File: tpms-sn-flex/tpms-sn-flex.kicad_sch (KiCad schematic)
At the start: 28 parts, among them IC1 NPP-301A-700AT, J1 Conn_02x04_Odd_Even, J2 Conn_01x04, J3 SMA Female, SW1 SW_Push, U1 STM32U031R8T6

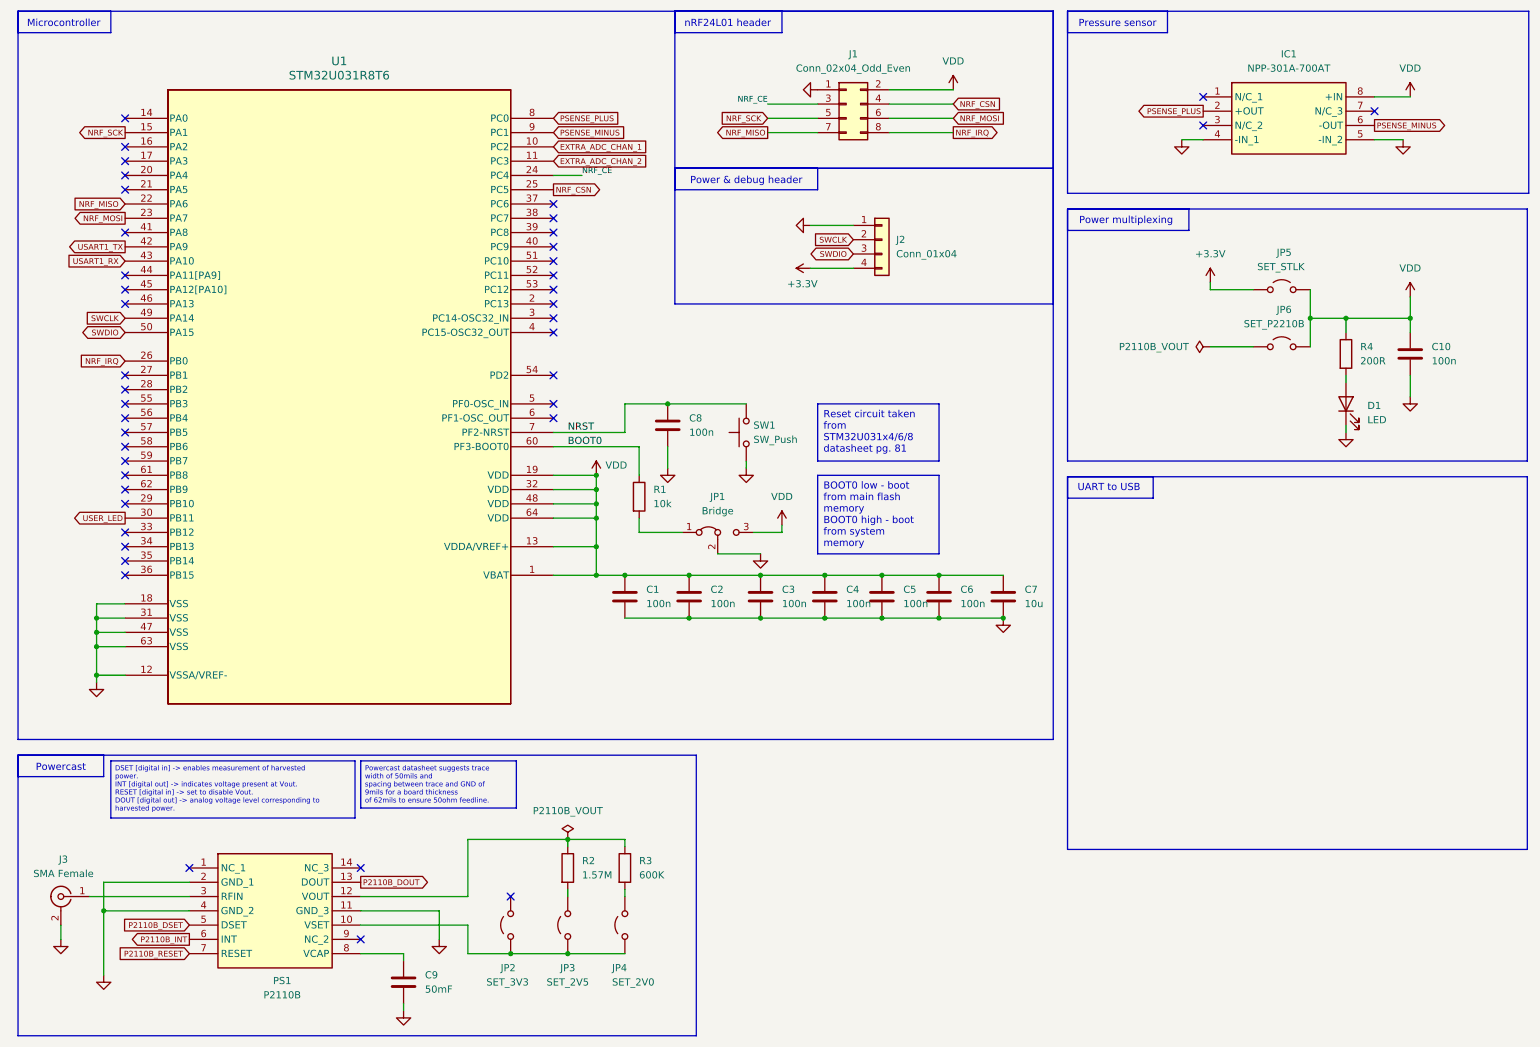
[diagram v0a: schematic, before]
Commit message: Add layout and routing for sensor node PCB rev 1
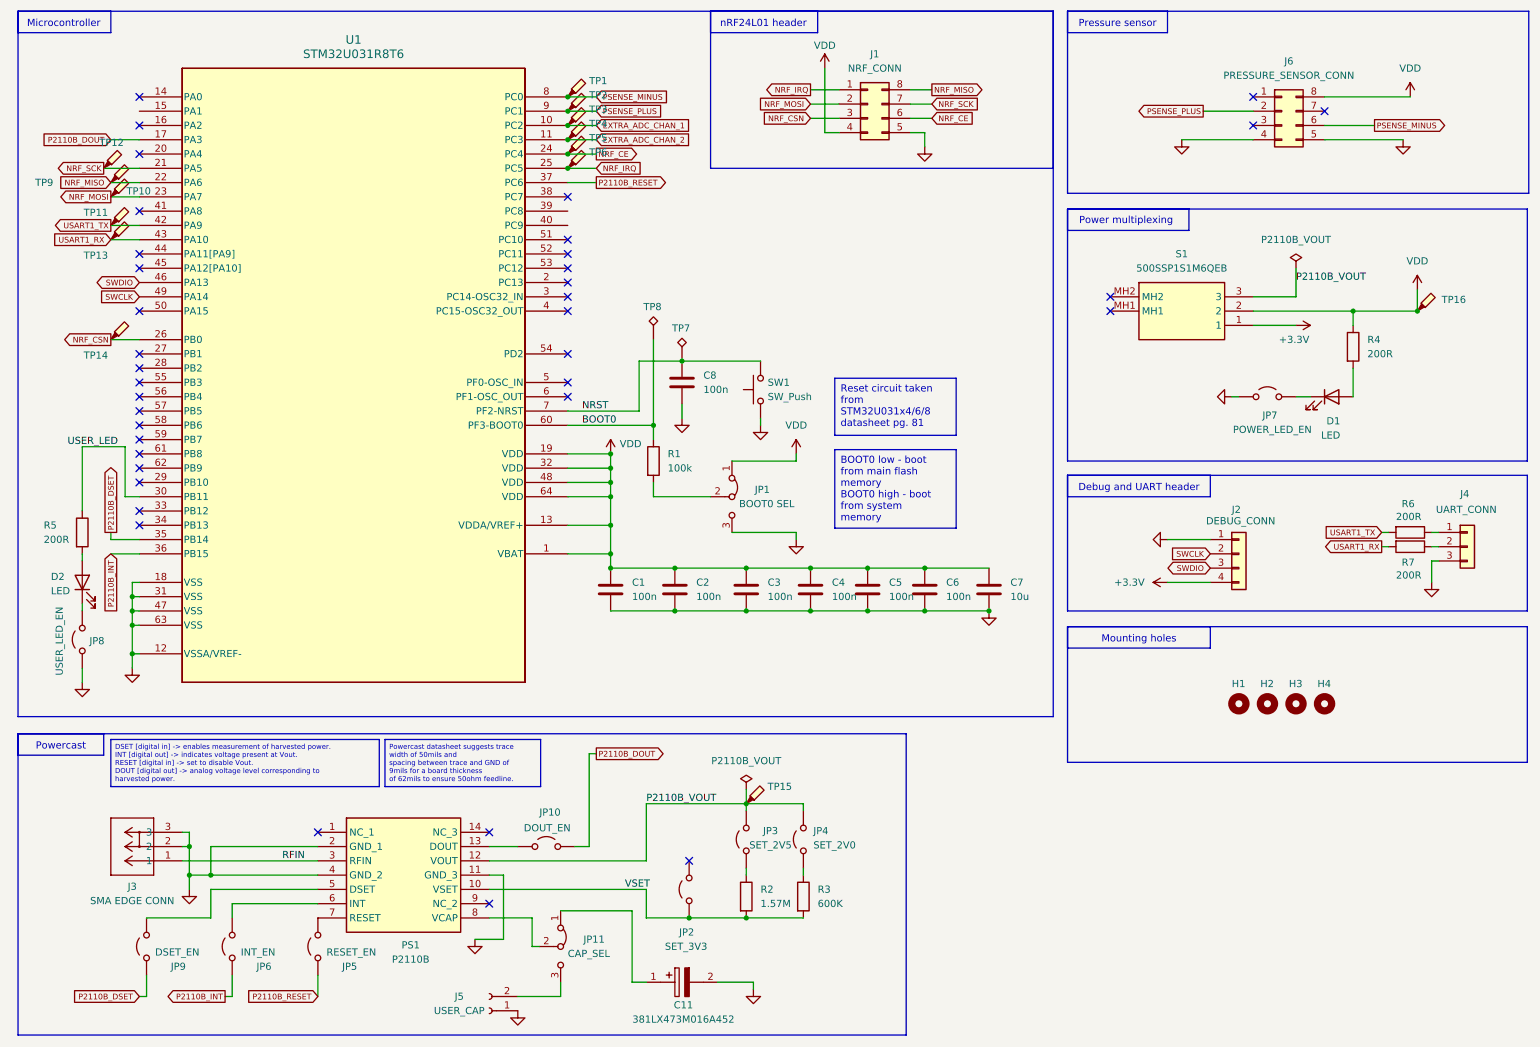
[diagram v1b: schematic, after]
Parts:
- removed C10: 100n, Capacitor_SMD:C_01005_0402Metric, symbol Device:C
- removed C9: 50mF, Capacitor_SMD:C_01005_0402Metric, symbol Device:C
- removed IC1: NPP-301A-700AT, libtpms:SOIC127P610X280-8N, symbol libtpms:NPP-301A-700AT
- removed J1: Conn_02x04_Odd_Even, Connector_PinHeader_2.54mm:PinHeader_2x04_P2.54mm_Vertical, symbol Connector_Generic:Conn_02x04_Odd_Even
- removed J3: SMA Female, symbol Connector:Conn_Coaxial
- added C11: 381LX473M016A452, libtpms:CAPPRD1000W200D3550H4700, symbol libtpms:381LX473M016A452
- added D2: LED, LED_SMD:LED_0402_1005Metric, symbol Device:LED
- added H1, H2, H3, H4: MountingHole, MountingHole:MountingHole_2.2mm_M2, symbol Mechanical:MountingHole
- added J1: NRF_CONN, Connector_PinSocket_2.54mm:PinSocket_2x04_P2.54mm_Vertical, symbol Connector_Generic:Conn_02x04_Counter_Clockwise
- added J3: SMA EDGE CONN, libtpms:CONN_73251-1150_MOL, symbol libtpms:732511150
- added J4: UART_CONN, Connector_PinHeader_2.54mm:PinHeader_1x03_P2.54mm_Vertical, symbol Connector_Generic:Conn_01x03
- added J5: USER_CAP, Connector_PinSocket_2.54mm:PinSocket_1x02_P2.54mm_Vertical, symbol Connector:Conn_01x02_Socket
- added J6: PRESSURE_SENSOR_CONN, libtpms:8-SOIC-DIP-8-ADAPTER, symbol Connector_Generic:Conn_02x04_Counter_Clockwise
- added JP10: DOUT_EN, Connector_PinHeader_2.54mm:PinHeader_1x02_P2.54mm_Vertical, symbol Jumper:Jumper_2_Open
- added JP11: CAP_SEL, Connector_PinHeader_2.54mm:PinHeader_1x03_P2.54mm_Vertical, symbol Jumper:Jumper_3_Bridged12
- added JP7: POWER_LED_EN, Connector_PinHeader_2.54mm:PinHeader_1x02_P2.54mm_Vertical, symbol Jumper:Jumper_2_Open
- added JP8: USER_LED_EN, Connector_PinHeader_2.54mm:PinHeader_1x02_P2.54mm_Vertical, symbol Jumper:Jumper_2_Open
- added JP9: DSET_EN, Connector_PinHeader_2.54mm:PinHeader_1x02_P2.54mm_Vertical, symbol Jumper:Jumper_2_Open
- added R5, R6, R7: 200R, Resistor_SMD:R_0603_1608Metric, symbol Device:R
- added S1: 500SSP1S1M6QEB, libtpms:500SSP1S1M6QEB, symbol libtpms:500SSP1S1M6QEB
- added TP1, TP2, TP3, TP4, TP5, TP6: TestPoint_Probe, TestPoint:TestPoint_Pad_2.0x2.0mm, symbol Connector:TestPoint_Probe
- added TP10, TP11, TP12, TP13, TP14, TP15, TP16, TP9: ~, TestPoint:TestPoint_Pad_2.0x2.0mm, symbol Connector:TestPoint_Probe
- added TP7, TP8: TestPoint_Alt, TestPoint:TestPoint_Pad_2.0x2.0mm, symbol Connector:TestPoint_Alt
- C7: footprint Capacitor_SMD:C_01005_0402Metric -> Capacitor_SMD:C_0201_0603Metric
- J2: value Conn_01x04 -> DEBUG_CONN
- JP1: value Bridge -> BOOT0 SEL; footprint TestPoint:TestPoint_Bridge_Pitch2.54mm_Drill1.0mm -> Connector_PinHeader_2.54mm:PinHeader_1x03_P2.54mm_Vertical
- JP2, JP3, JP4: footprint (none) -> Connector_PinHeader_2.54mm:PinHeader_1x02_P2.54mm_Vertical
- JP5: value SET_STLK -> RESET_EN; footprint (none) -> Connector_PinHeader_2.54mm:PinHeader_1x02_P2.54mm_Vertical
- JP6: value SET_P2210B -> INT_EN; footprint (none) -> Connector_PinHeader_2.54mm:PinHeader_1x02_P2.54mm_Vertical
- PS1: footprint P2110B -> libtpms:P2110B
- R1: value 10k -> 100k; footprint Resistor_SMD:R_0402_1005Metric -> Resistor_SMD:R_0603_1608Metric
- R2, R3, R4: footprint Resistor_SMD:R_0402_1005Metric -> Resistor_SMD:R_0603_1608Metric
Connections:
- net +3.3V: now also S1.1; no longer JP5.1 (A)
- net BOOT0: now also TP8.1
- net EXTRA_ADC_CHAN_1: now also TP3.1
- net EXTRA_ADC_CHAN_2: now also TP4.1
- net GND: now also JP1.3 (B), C11.2, J1.5 (Pin_5), J3.2, J3.3, J4.3 (Pin_3), J5.1 (Pin_1), J6.4 (Pin_4), J6.5 (Pin_5), JP7.1 (A), JP8.1 (A); no longer D1.1 (K), JP1.2 (C)
- net NRF_CE: now also J1.6 (Pin_6), TP5.1
- net NRF_CSN: now also U1.26 (PB0), J1.3 (Pin_3), TP14.1; no longer U1.25 (PC5)
- net NRF_IRQ: now also U1.25 (PC5), J1.1 (Pin_1), TP6.1; no longer U1.26 (PB0)
- net NRF_MISO: now also J1.8 (Pin_8), TP9.1
- net NRF_MOSI: now also J1.2 (Pin_2), TP10.1
- net NRF_SCK: now also U1.21 (PA5), J1.7 (Pin_7), TP12.1; no longer U1.15 (PA1)
- net NRST: now also TP7.1
- net P2110B_DOUT: now also U1.17 (PA3), JP10.2 (B); no longer PS1.13 (DOUT)
- net P2110B_DSET: now also U1.35 (PB14), JP9.1 (A); no longer PS1.5 (DSET)
- net P2110B_INT: now also JP6.1 (A), U1.36 (PB15); no longer PS1.6 (INT)
- net P2110B_RESET: now also JP5.1 (A), U1.37 (PC6); no longer PS1.7 (RESET)
- net PSENSE_MINUS: now also U1.8 (PC0), J6.6 (Pin_6), TP1.1; no longer U1.9 (PC1)
- net PSENSE_PLUS: now also U1.9 (PC1), J6.2 (Pin_2), TP2.1; no longer U1.8 (PC0)
- net SWDIO: now also U1.46 (PA13); no longer U1.50 (PA15)
- net USART1_RX: now also R7.2, TP13.1
- net USART1_TX: now also R6.2, TP11.1
- net USER_LED: now also R5.1
- net VDD: now also JP1.1 (A), J1.4 (Pin_4), J6.8 (Pin_8), S1.2, TP16.1; no longer JP1.3 (B), JP5.2 (B), JP6.2 (B)
- net VSET: now reaches JP2.1 (A), PS1.10 (VSET)
- net VSET: now also R2.2, R3.2; no longer JP3.1 (A), JP4.1 (A)
- net RFIN: now reaches PS1.3 (RFIN)
- net RFIN: now also J3.1
- net at PS1.8 (VCAP): now also JP11.2 (C)
- net P2110B_VOUT: now reaches JP3.2 (B)
- net P2110B_VOUT: now also JP4.2 (B), PS1.12 (VOUT), S1.3, TP15.1; no longer R2.2
- net at R1.2: now also JP1.2 (C); no longer JP1.1 (A)
- new net: D2.1 (K), JP8.2 (B)
- new net: D2.2 (A), R5.2
- new net: JP5.2 (B), PS1.7 (RESET)
- new net: JP9.2 (B), PS1.5 (DSET)
- new net: JP6.2 (B), PS1.6 (INT)
- new net: C11.1, JP11.1 (A)
- new net: JP10.1 (A), PS1.13 (DOUT)
- new net: J4.2 (Pin_2), R7.1
- new net: JP3.1 (A), R2.1
- new net: J4.1 (Pin_1), R6.1
- new net: D1.1 (K), JP7.2 (B)
- new net: J5.2 (Pin_2), JP11.3 (B)
- new net: JP4.1 (A), R3.1
- no-connect marks 43 -> 38
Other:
- note added: "Debug and UART header"
- note added: "Mounting holes"
- note removed: "Power & debug header"
- note removed: "UART to USB"
- company: (none) -> TL-81
- title: (none) -> Sensor Node
- moved on the sheet: C1, C2, C3, C4, C5, C6, C7, C8, D1, J2, JP1, JP2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
